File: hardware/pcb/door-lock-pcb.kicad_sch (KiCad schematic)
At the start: 40 parts, among them J1 105162-0001, J2 Conn_01x08, J3 Conn_01x03, J4 Conn_01x04, J7 JST XH, Q1 SI2308DS, U1 ESP32-DEVKIT-V1, U2 DS1307Z+, U3 MP1470, Y1 Crystal

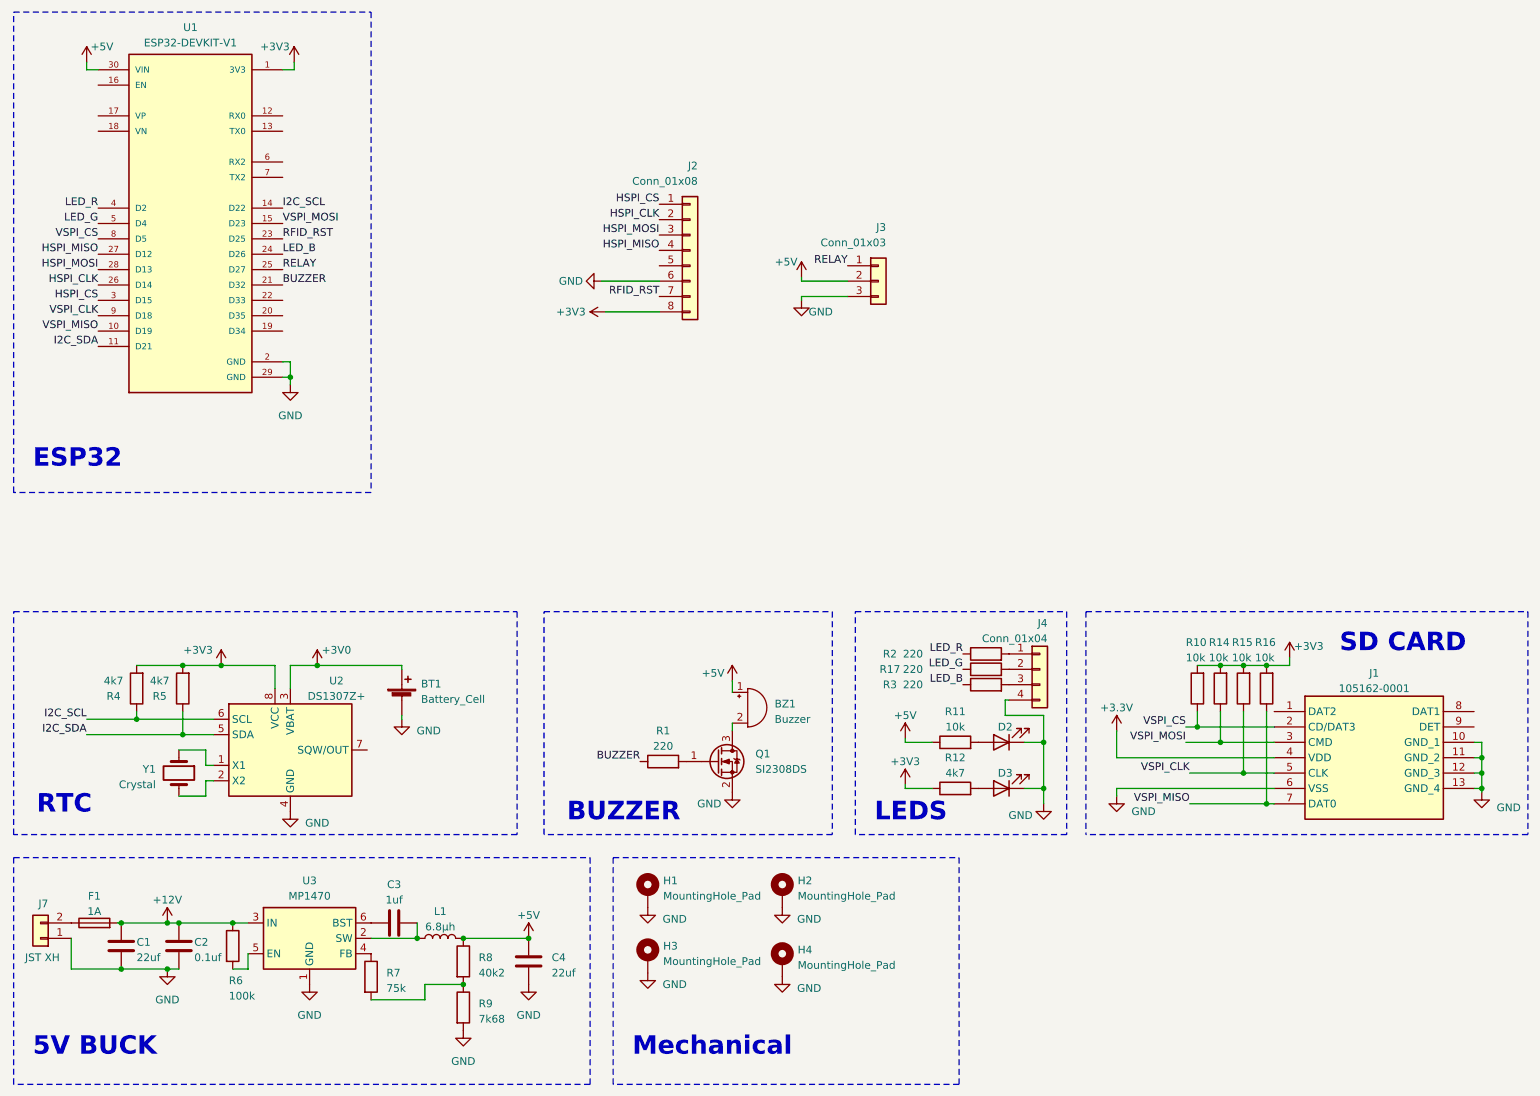
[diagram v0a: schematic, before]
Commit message: added a mosfet for the solenoid + upgraded he fuse
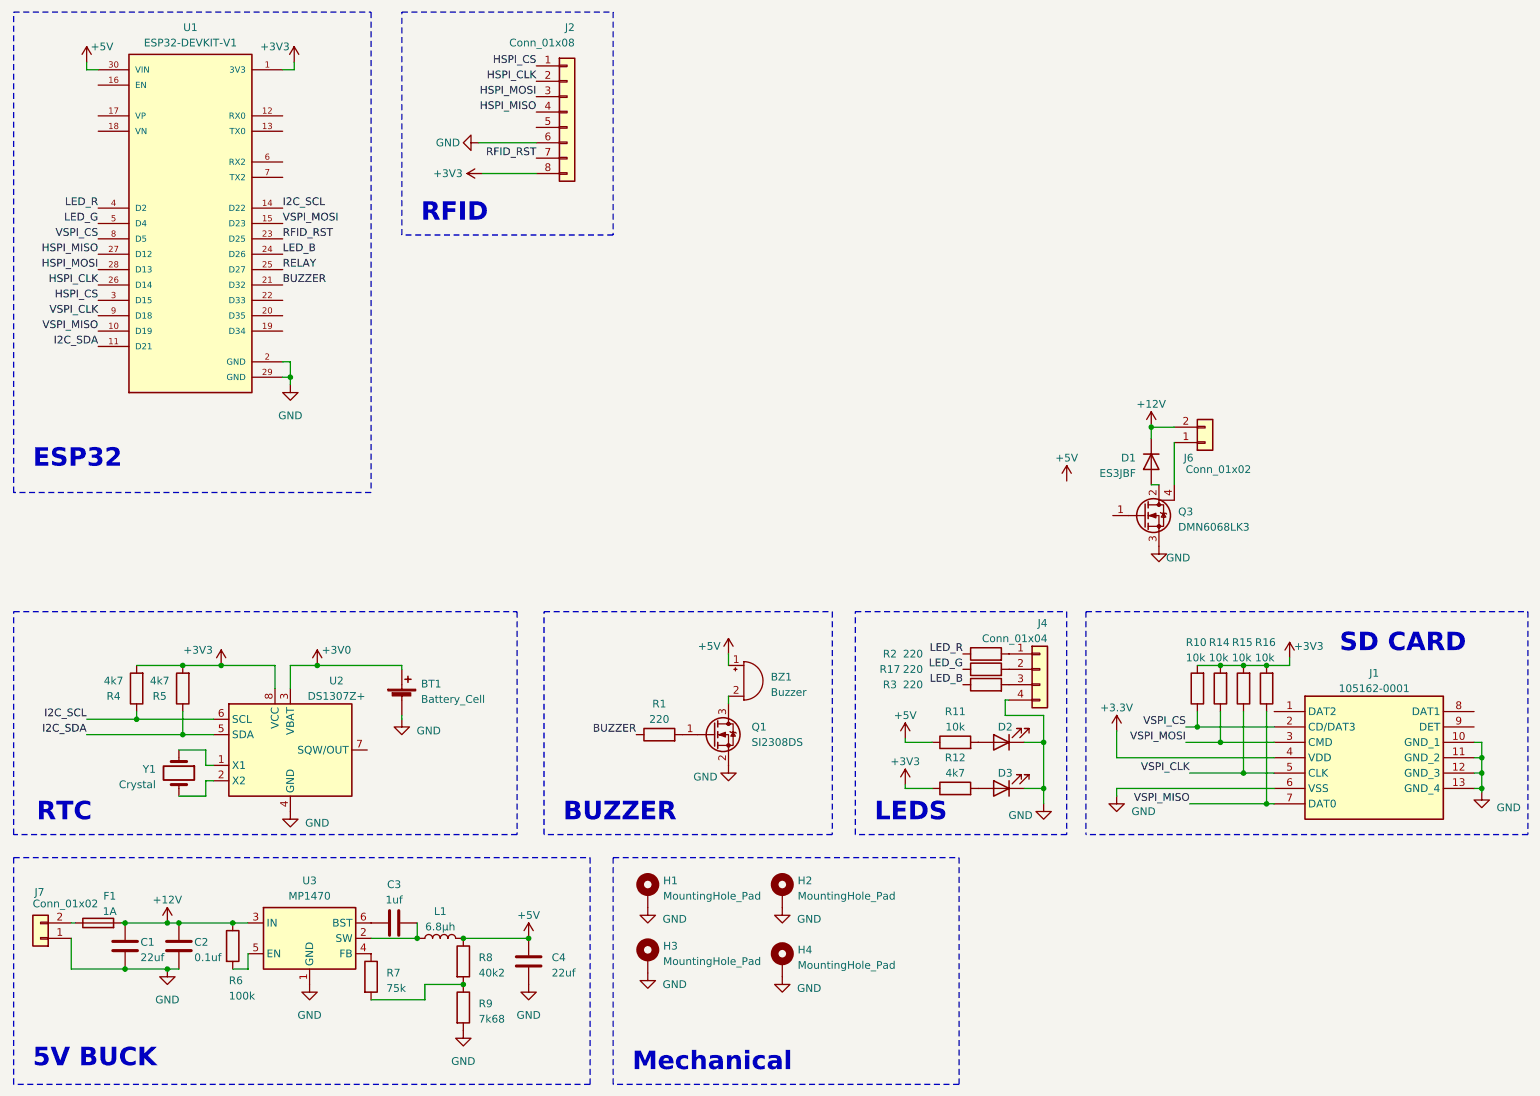
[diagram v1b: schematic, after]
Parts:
- removed J3: Conn_01x03, Connector_JST:JST_XH_B3B-XH-A_1x03_P2.50mm_Vertical, symbol Connector_Generic:Conn_01x03
- added D1: ES3JBF, Diode_SMD:D_SMC, symbol Device:D
- added J6: Conn_01x02, Connector_JST:JST_XH_B2B-XH-A_1x02_P2.50mm_Vertical, symbol Connector_Generic:Conn_01x02
- added Q3: DMN6068LK3, Package_TO_SOT_SMD:TO-252-3_TabPin4, symbol Device:Q_NMOS_GDSD
- F1: footprint Fuse:Fuse_1206_3216Metric -> C3131:FUSE-TH_L22.6-W9.0
- J7: value JST XH -> Conn_01x02
- L1: footprint Inductor_SMD:L_Changjiang_FNR8040S -> C5189755:IND-SMD_L7.2-W6.6_GPSR07X0
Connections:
- net +12V: now also D1.1 (K), J6.2 (Pin_2)
- net GND: now also Q3.3 (S)
- new net: J6.1 (Pin_1), Q3.4 (D)
- new net: D1.2 (A), Q3.2 (D)
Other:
- note added: "RFID"
- moved on the sheet: BZ1, C1, F1, J2, Q1, R1

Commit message: finished rev 1 of pcb + ported MFRC522 library to ESP-IDF + finished the BOM
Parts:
- removed BZ1: Buzzer, Buzzer_Beeper:Buzzer_12x9.5RM7.6, symbol Device:Buzzer
- added BUZZER1: FT12095-G/12V, C781867:BUZ-TH_BD12.0-P7.60-D0.6-FD, symbol C781867:FT12095-G_12V
- added C6, C7: 100, Capacitor_SMD:CP_Elec_6.3x5.4, symbol Device:C_Polarized_Small
- added C8: 1uf, Capacitor_SMD:C_0805_2012Metric_Pad1.18x1.45mm_HandSolder, symbol Device:C
- added D4: ~, LED_SMD:LED_0805_2012Metric_Pad1.15x1.40mm_HandSolder, symbol Device:LED
- added Q2: BC817DPN, Package_TO_SOT_SMD:SOT-363_SC-70-6, symbol Device:Q_Dual_NPN_PNP_E1B1C2E2B2C1
- added R13, R18: 220, Resistor_SMD:R_0805_2012Metric_Pad1.20x1.40mm_HandSolder, symbol Device:R
- added R19: 4k7, Resistor_SMD:R_0805_2012Metric_Pad1.20x1.40mm_HandSolder, symbol Device:R
- BT1: LCSC (none) -> C70381
- D1: LCSC (none) -> C3011135
- F1: LCSC (none) -> C3131
- J1: LCSC (none) -> C393941
- L1: LCSC (none) -> C5189755
- Q3: LCSC (none) -> C154756
- U2: LCSC (none) -> C5145427
- U3: LCSC (none) -> C558426
- Y1: LCSC (none) -> C2992632
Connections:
- net +12V: now also BUZZER1.1, C6.1, C7.1, Q2.3 (C2)
- net +3V3: now also C8.1
- net GND: now also C6.2, C7.2, C8.2, D4.1 (K), Q2.1 (E1)
- net HSPI_CLK: now also J1.5 (CLK), R15.1; no longer J2.2 (Pin_2)
- net HSPI_CS: now also J1.2 (CD/DAT3), R10.1; no longer J2.1 (Pin_1)
- net HSPI_MISO: now also J1.7 (DAT0), R16.1; no longer J2.4 (Pin_4)
- net HSPI_MOSI: now also J1.3 (CMD), R14.1; no longer J2.3 (Pin_3)
- net RELAY: now also R18.1, R19.1
- net VSPI_CLK: now also J2.2 (Pin_2); no longer J1.5 (CLK), R15.1
- net VSPI_CS: now also J2.1 (Pin_1); no longer J1.2 (CD/DAT3), R10.1
- net VSPI_MISO: now also J2.4 (Pin_4); no longer J1.7 (DAT0), R16.1
- net VSPI_MOSI: now also J2.3 (Pin_3); no longer J1.3 (CMD), R14.1
- net at Q1.3 (D): now also BUZZER1.2
- net at Q3.1 (G): now also R13.2
- net IRQ: now reaches U1.19 (D34)
- net IRQ: now also J2.5 (Pin_5)
- new net: Q2.2 (B1), Q2.5 (B2), R18.2
- new net: Q2.4 (E2), Q2.6 (C1), R13.1
- new net: D4.2 (A), R19.2
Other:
- note added: "RELAY"
- moved on the sheet: D1, D2, J4, J6, Q1, Q3, R1, R11, R17, R2, R3
